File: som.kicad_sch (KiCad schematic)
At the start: 33 parts, among them J15 Bus_DDR4_SODIMM_CUSTOM_Jetson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, U4 NTS0102

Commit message: Power routing, CSI length matching, cleanup
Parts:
- removed R31, R80: 200k, Resistor_SMD:R_0402_1005Metric, symbol Device:R_Small
- added R103, R104: 0R, Resistor_SMD:R_0402_1005Metric, symbol Device:R_Small
- added TP26, TP27: TP_0.75mm_SMD, JetsonCarrier:TP_SMD_0.75mm, symbol Connector:TestPoint
- U4: footprint JetsonCarrier:XSON-8_1x1.95mm_P0.5mm -> Argus-IC:NXP_XSON-8
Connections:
- net at J15.143 (CAN_RX): now also R103.1
- net at J15.145 (CAN_TX): now also R104.1
- net SPI0_MOSI: now reaches J15.89 (SPI0_MOSI)
- net SPI0_SCK: now reaches J15.91 (SPI0_SCK)
- net SPI0_MISO: now reaches J15.93 (SPI0_MISO)
- net ~{SPI0_CS}: now reaches J15.95 (~{SPI0_CS0})
- net I2C1_SCL: no longer names the net of J15.189 (I2C1_SCL)
- net I2C1_SDA: no longer names the net of J15.191 (I2C1_SDA)
- net SYS_SCL: no longer names the net of J15.185 (I2C0_SCL)
- net SYS_SDA: no longer names the net of J15.187 (I2C0_SDA)
- net UART1_RXD: no longer names the net of J15.205 (UART1_RXD)
- net UART1_RXD: now also TP27.1
- net UART1_TXD: no longer names the net of J15.203 (UART1_TXD)
- net UART1_TXD: now also TP26.1
- net USBC0_FLG renamed USB2_FLG
- net USBC0_PEN renamed USB2_PEN
- net USBC1_FLG renamed USB1_FLG
- net USBC1_PEN renamed USB1_PEN
- net ~{USBC0_INT}: no longer names the net of J15.211 (GPIO09/AUD_MCLK)
- net ~{USBC1_INT}: no longer names the net of J15.212 (GPIO10)
- new net CAN_RXD: R103.2
- new net CAN_TXD: R104.2
- no-connect marks 70 -> 74

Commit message: Layout cleanup, silk
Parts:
- removed TP26, TP27: TP_0.75mm_SMD, JetsonCarrier:TP_SMD_0.75mm, symbol Connector:TestPoint
- TP25, TP7: footprint JetsonCarrier:TP_SMD_0.75mm -> TestPoint:TestPoint_Pad_D1.0mm
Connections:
- no-connect marks 74 -> 76

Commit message: route all diff pairs, length tuning
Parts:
- removed U4: NTS0102, Argus-IC:NXP_XSON-8, symbol JetsonCarrier:NTS0102
- added U1: NTS0102, Argus-IC:NXP_XSON-8, symbol Argus-IC:NTS0102
- R1: renamed from R174; footprint Resistor_SMD:R_0402_1005Metric -> Resistor_SMD:R_0603_1608Metric
- renumbered C46 to C5, C35 to C6, C36 to C7, C37 to C8, C38 to C9, D21 to D1, D15 to D2, J15 to J1, R97 to R10, R98 to R11, R103 to R12, R104 to R13, R11 to R14, R12 to R15, R4 to R2, R5 to R3, R84 to R4, R92 to R5, R93 to R6, R94 to R7, R95 to R8, R96 to R9, TP7 to TP1, TP25 to TP2
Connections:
- net +1V8: now also U1.3 (VCC_{A}), U1.6 (OE)
- net +3V3: now also U1.7 (VCC_{B})
- net DEBUG_RXD: now also U1.8 (B_{1})
- net DEBUG_RXD_1V8: now also U1.5 (A_{1})
- net DEBUG_TXD: now also U1.1 (B_{2})
- net DEBUG_TXD_1V8: now also U1.4 (A_{2})
- net GND: now also U1.2 (GND)
- no-connect marks 76 -> 72

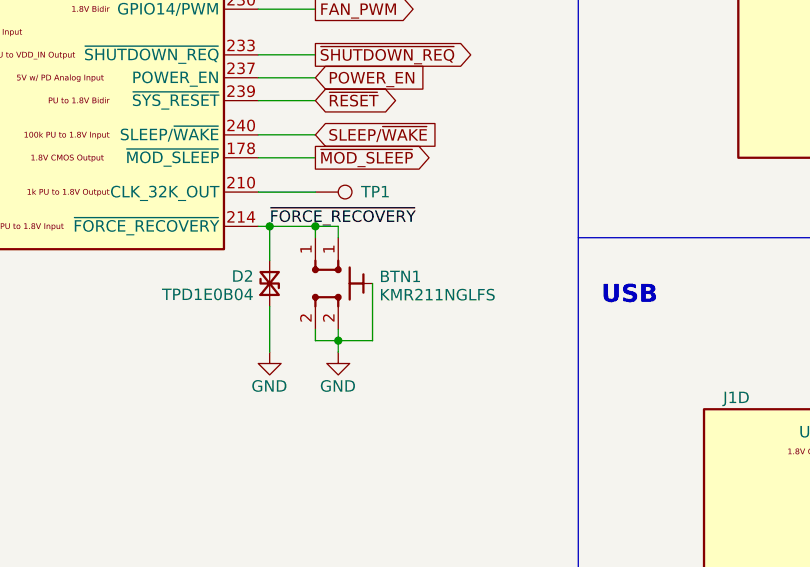
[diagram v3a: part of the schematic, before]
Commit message: Move switch up top
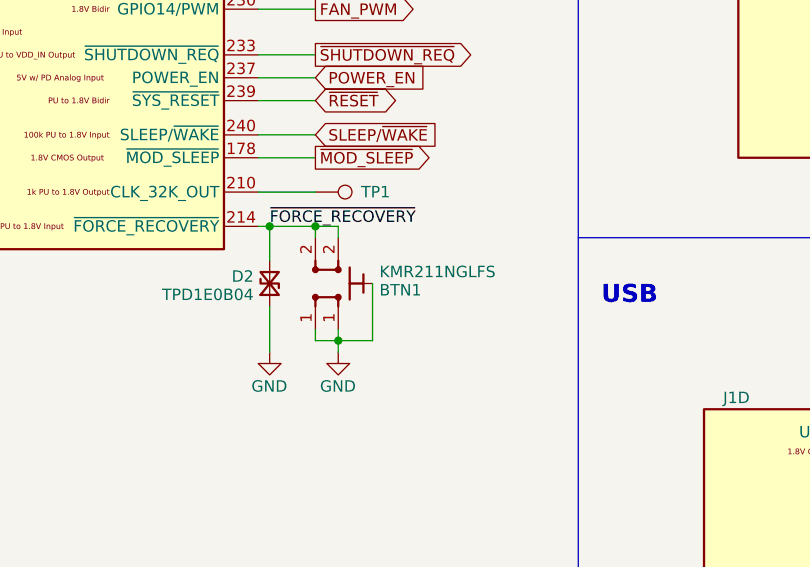
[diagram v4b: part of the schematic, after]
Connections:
- net GND: now also BTN1.1; no longer BTN1.2
- net ~{FORCE_RECOVERY}: now also BTN1.2; no longer BTN1.1
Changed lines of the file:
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@@
 	(symbol
 		(lib_id "JetsonCarrier:SW_KMR211NGLFS_SMD")
-		(at 113.03 165.1 270)
+		(at 113.03 175.26 270)
+		(mirror x)
 		(unit 1)
 		(body_style 1)
@@
 		)
 		(property "Value" "KMR211NGLFS"
-			(at 117.602 172.212 90)
+			(at 117.602 168.148 90)
 			(show_name no)
 			(do_not_autoplace no)
@@
 		)
 		(property "Description" ""
-			(at 113.03 165.1 0)
+			(at 113.03 175.26 0)
 			(hide yes)
 			(show_name no)
@@
 		)
 		(property "MPN" "C221676"
-			(at 123.0122 170.0784 0)
+			(at 123.0122 170.2816 0)
 			(hide yes)
 			(show_name no)

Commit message: Move buttons up top, shorten reset trace, DRC
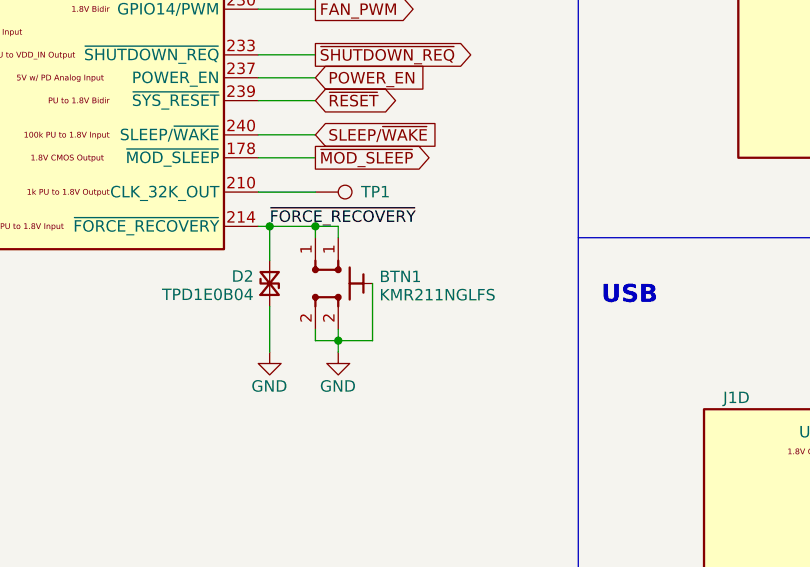
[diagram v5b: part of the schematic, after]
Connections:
- net GND: now also BTN1.2; no longer BTN1.1
- net ~{FORCE_RECOVERY}: now also BTN1.1; no longer BTN1.2
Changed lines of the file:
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@@
 	(symbol
 		(lib_id "JetsonCarrier:SW_KMR211NGLFS_SMD")
-		(at 113.03 175.26 270)
-		(mirror x)
+		(at 113.03 165.1 270)
 		(unit 1)
 		(body_style 1)
@@
 		)
 		(property "Value" "KMR211NGLFS"
-			(at 117.602 168.148 90)
+			(at 117.602 172.212 90)
 			(show_name no)
 			(do_not_autoplace no)
@@
 		)
 		(property "Description" ""
-			(at 113.03 175.26 0)
+			(at 113.03 165.1 0)
 			(hide yes)
 			(show_name no)
@@
 		)
 		(property "MPN" "C221676"
-			(at 123.0122 170.2816 0)
+			(at 123.0122 170.0784 0)
 			(hide yes)
 			(show_name no)

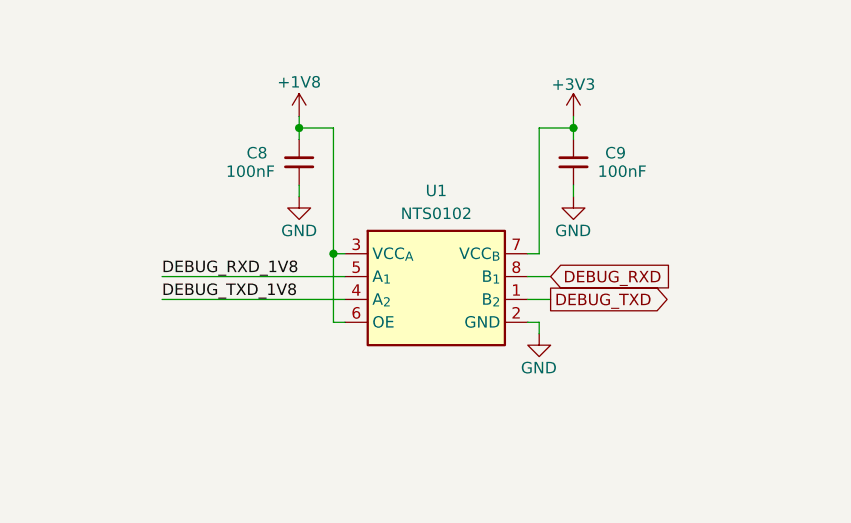
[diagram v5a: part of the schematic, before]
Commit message: Move parts under SoM to bottom for thinner module connector
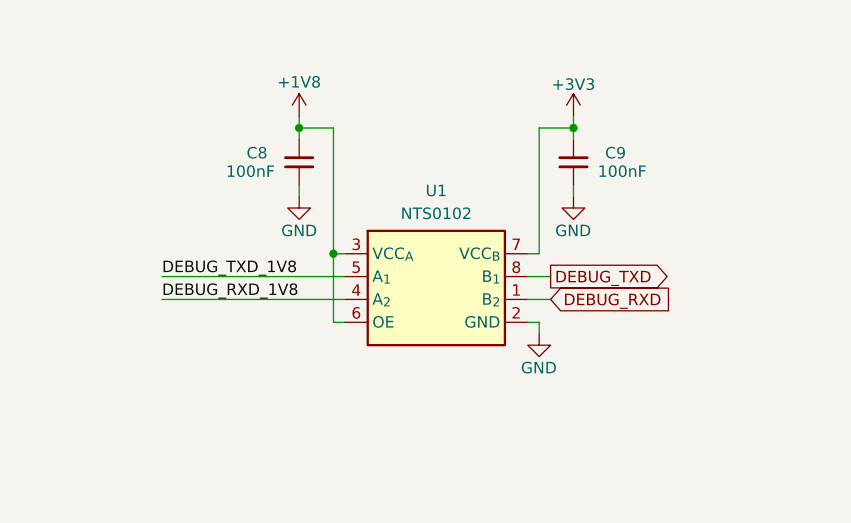
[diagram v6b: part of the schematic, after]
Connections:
- net DEBUG_RXD: now also U1.1 (B_{2}); no longer U1.8 (B_{1})
- net DEBUG_RXD_1V8: now also U1.4 (A_{2}); no longer U1.5 (A_{1})
- net DEBUG_TXD: now also U1.8 (B_{1}); no longer U1.1 (B_{2})
- net DEBUG_TXD_1V8: now also U1.5 (A_{1}); no longer U1.4 (A_{2})
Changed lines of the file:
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@@
 	)
 	(label "DEBUG_TXD_1V8"
-		(at 45.72 260.35 0)
+		(at 45.72 257.81 0)
 		(effects
 			(font
@@
 	)
 	(label "DEBUG_RXD_1V8"
-		(at 45.72 257.81 0)
+		(at 45.72 260.35 0)
 		(effects
 			(font
@@
 	(global_label "DEBUG_TXD"
 		(shape output)
-		(at 88.9 260.35 0)
-		(effects
-			(font
-				(size 1.27 1.27)
-			)
-			(justify left)
-		)
-		(property "Intersheetrefs" "${INTERSHEET_REFS}"
-			(at 102.87 260.35 0)
+		(at 88.9 257.81 0)
+		(effects
+			(font
+				(size 1.27 1.27)
+			)
+			(justify left)
+		)
+		(property "Intersheetrefs" "${INTERSHEET_REFS}"
+			(at 102.87 257.81 0)
 			(show_name no)
 			(do_not_autoplace no)
@@
 	(global_label "DEBUG_RXD"
 		(shape input)
-		(at 88.9 257.81 0)
-		(effects
-			(font
-				(size 1.27 1.27)
-			)
-			(justify left)
-		)
-		(property "Intersheetrefs" "${INTERSHEET_REFS}"
-			(at 102.87 257.81 0)
-			(show_name no)
-			(do_not_autoplace no)
+		(at 88.9 260.35 0)
+		(effects
+			(font
+				(size 1.27 1.27)
+			)
+			(justify left)
+		)
+		(property "Intersheetrefs" "${INTERSHEET_REFS}"
+			(at 102.87 260.35 0)
+			(show_name no)
+			(do_not_autoplace no)

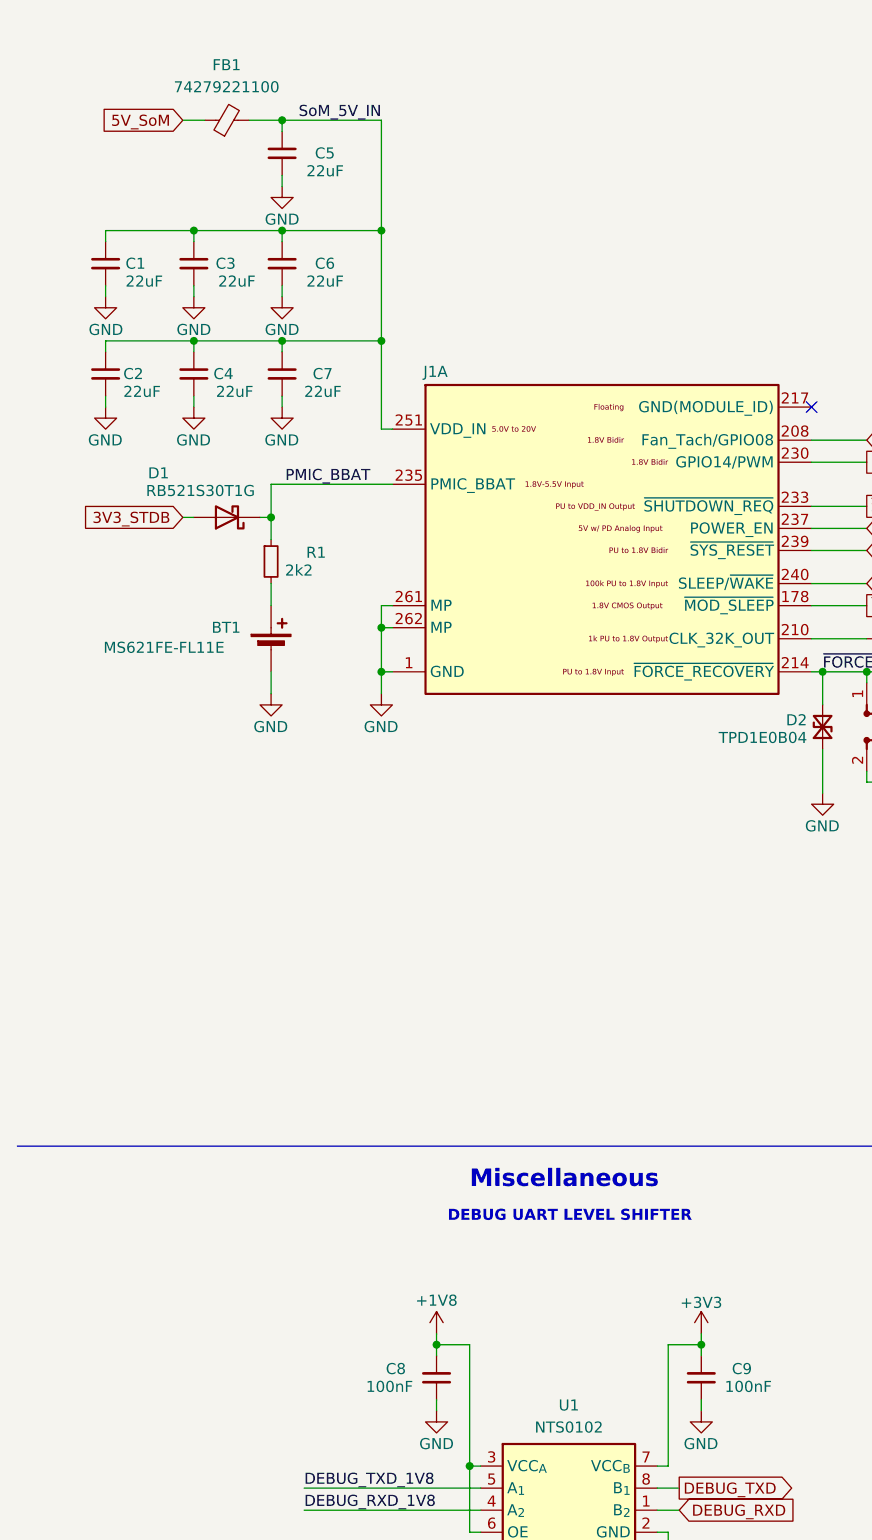
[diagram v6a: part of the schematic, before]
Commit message: Replace current monitor w/ INA226 (addr = 0x42)
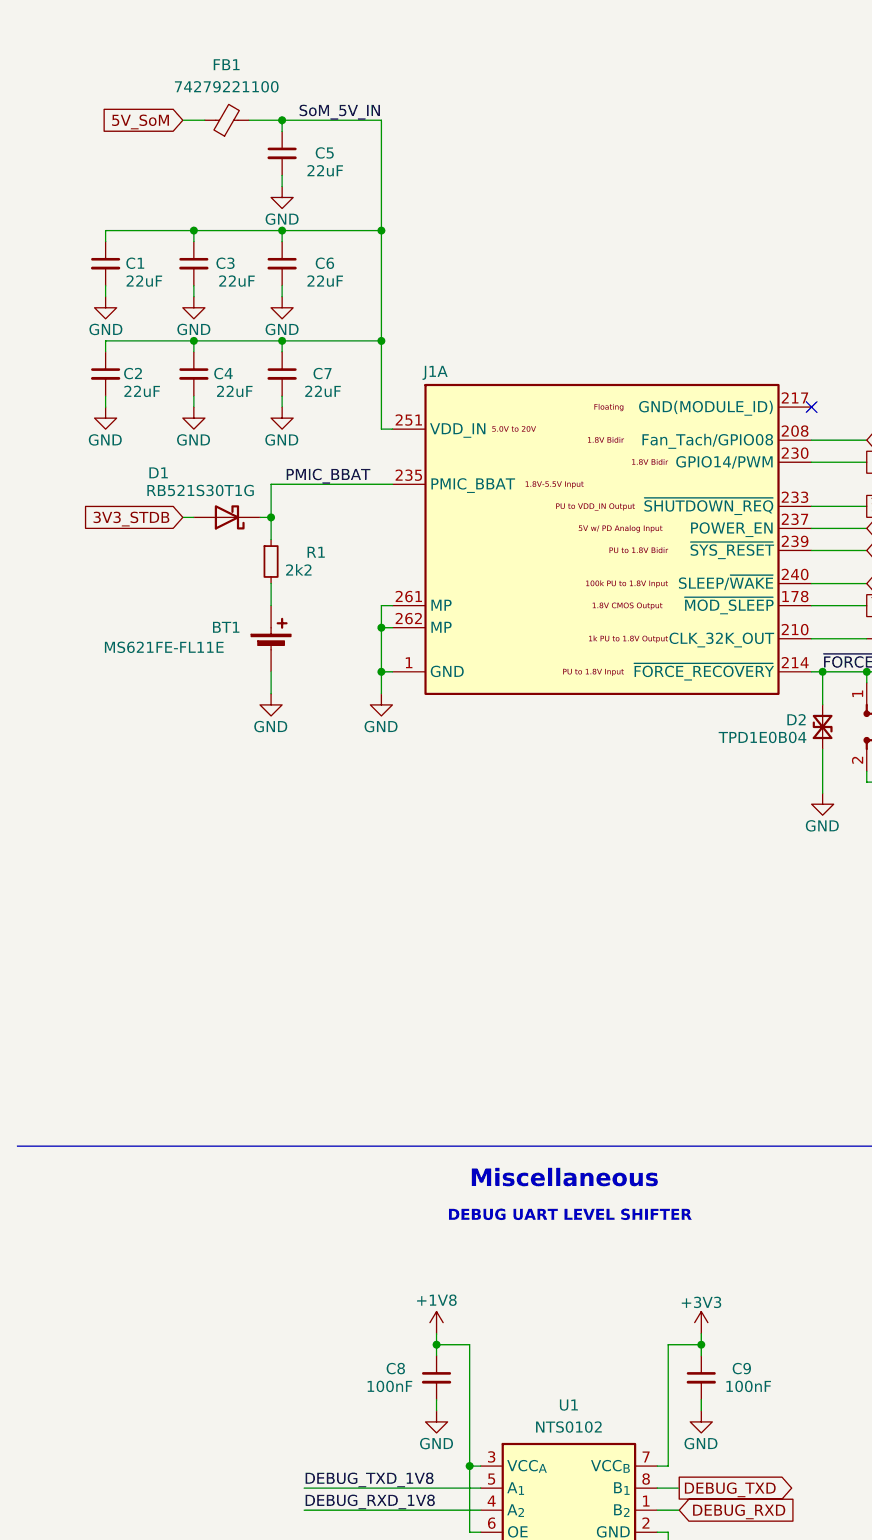
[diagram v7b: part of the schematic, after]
